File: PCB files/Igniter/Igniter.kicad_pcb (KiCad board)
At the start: 2 copper layers, 124.9 x 69.6 mm, 56 parts, among them IC1 74HC4050, J1 PT, J10 SL3, J11 SL4, J12 SL5, J13 Micro_SD_Card, J2 PT, J3 PT, J4 PT, J5 Battery, J6 Ignition Coil +, J7 Ignition coil -, J8 SL1, J9 SL2, Q1 N MOSFET, Q2 N MOSFET, Q3 N MOSFET, Q4 N MOSFET, Q5 N MOSFET, Q6 N MOSFET, SW1 ARM, U2 FDS8984, U3 FDS8984, U4 FDS8984

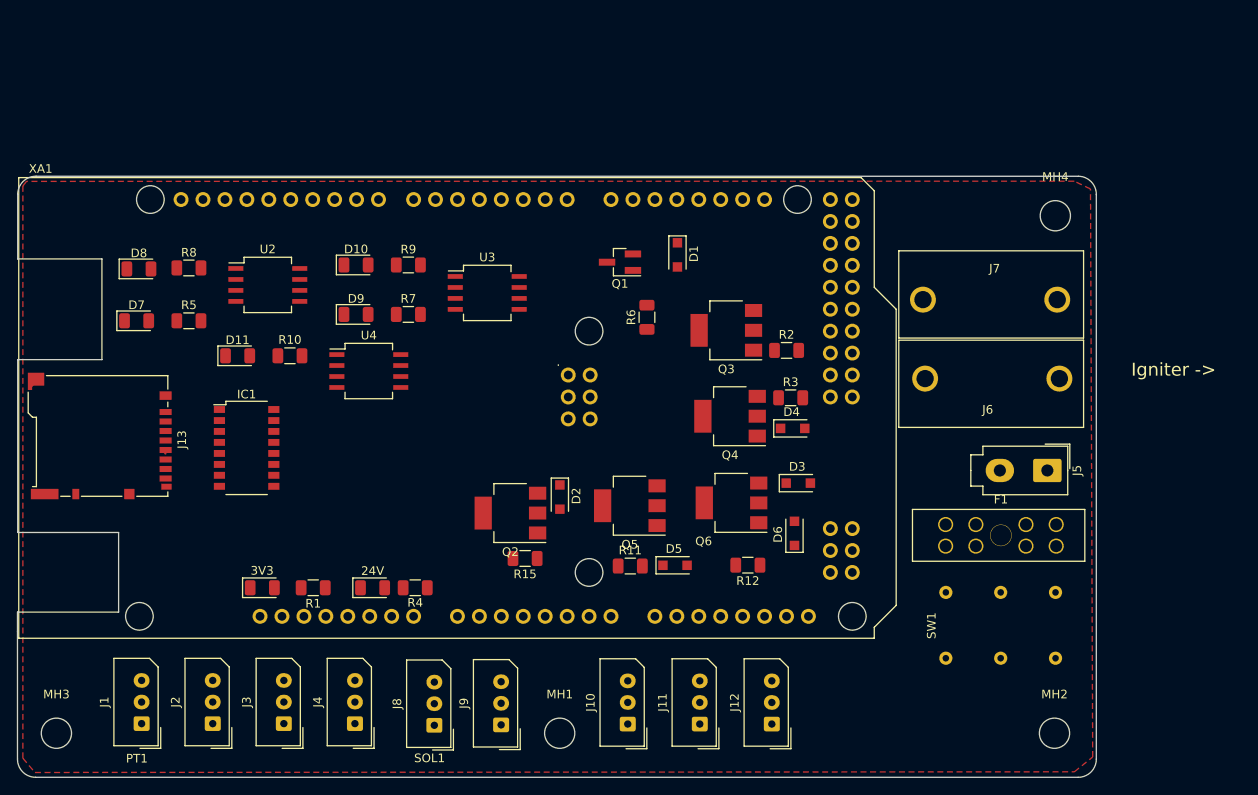
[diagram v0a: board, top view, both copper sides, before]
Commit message: 1/9/2019
-Set design rules to match with jlcpcb
-Began laying out power and some signal traces
-Changed FET symbol to 4pin to match sot223 footprint
Removed unused Arduino pins: (5V3,5V4,D22-D39)
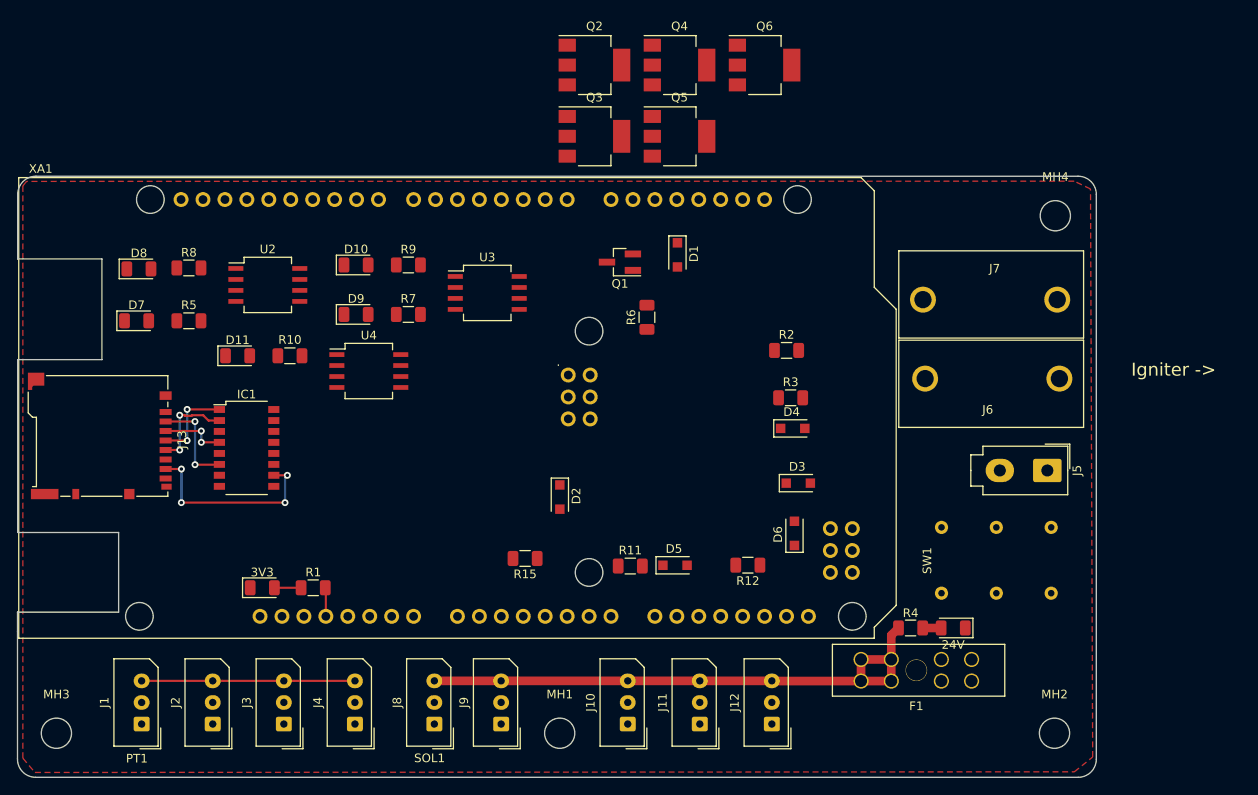
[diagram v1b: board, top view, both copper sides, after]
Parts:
- Q2, Q3, Q4, Q5, Q6: value N MOSFET -> Q_NMOS_GDSD
- moved D13 67.4 mm to (193.4, 138.4), turned to 180 degrees
- moved R4 57.6 mm to (188.5, 138.4), turned to 180 degrees
- moved Q2 52.8 mm to (151.9, 73.3), turned to 0 degrees
- moved Q6 50.8 mm to (171.6, 73.3), turned to 0 degrees
- moved Q5 43.2 mm to (161.7, 81.5), turned to 0 degrees
- moved Q4 41.1 mm to (161.7, 73.3), turned to 0 degrees
- moved Q3 27.2 mm to (151.9, 81.5), turned to 0 degrees
- moved F1 18.4 mm to (189.2, 143.3), turned to 0 degrees
- moved SW1 7.55 mm to (198.4, 130.6)
- moved J8 0.14 mm to (133.4, 149.6)
- moved J9 0.10 mm to (141.1, 149.6)
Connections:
- Q2 pad 4: (no net) -> Net-(D2-Pad2)
- Q3 pad 4: (no net) -> Net-(D3-Pad2)
- Q4 pad 4: (no net) -> Net-(D4-Pad2)
- Q5 pad 4: (no net) -> Net-(D5-Pad2)
- Q6 pad 4: (no net) -> Net-(D6-Pad2)
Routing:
- net +24V: track 0.00 -> 90.1 mm
- net Net-(IC1-Pad10): track 0.00 -> 22.6 mm, vias 0 -> 4
- net +3V3: track 0.11 -> 13.2 mm, vias 0 -> 2
- net Net-(IC1-Pad6): track 0.00 -> 11.2 mm, vias 0 -> 2
- net Net-(IC1-Pad2): track 0.00 -> 10.6 mm, vias 0 -> 2
- net Net-(IC1-Pad4): track 0.00 -> 7.54 mm, vias 0 -> 2
- net Net-(D12-Pad2): track 0.00 -> 3.09 mm
- net Net-(D13-Pad2): track 0.00 -> 2.14 mm
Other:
- board text added: "Trace direction: FRONT = Horizontal BACK = Vertical"
- board text removed: "Trace direction: FRONT = Vertical BACK = Horizontal"

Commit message: 1/14/2020
-Continued work on board routing
-Changed igniter connector footprint to have two pins to match banana jack connector
-Created GND plane on bottom layer
-Created footprint for rocker switch
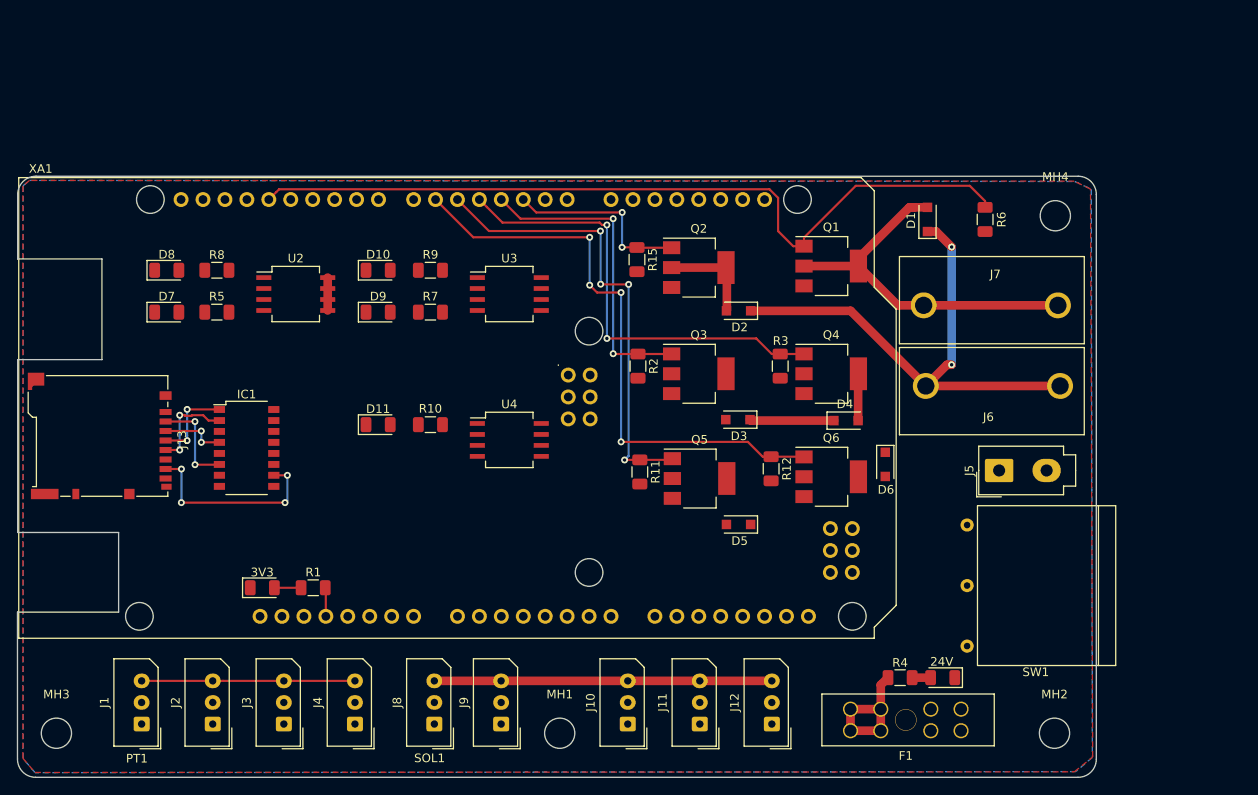
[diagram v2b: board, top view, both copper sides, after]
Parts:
- J6: value Ignition Coil + -> COIL
- J7: value Ignition coil - -> COIL
- Q1: value N MOSFET -> IGN; footprint Package_TO_SOT_SMD:SOT-23_Handsoldering -> Package_TO_SOT_SMD:SOT-223
- SW1: footprint IgniterFootprints:C&K_S101031MS02Q -> IgniterCustom:R1966ABLKBLKFR-SPST
- moved Q6 48.3 mm to (179.3, 120.9)
- moved R6 40.8 mm to (197.1, 91.1)
- moved Q4 39.8 mm to (179.3, 109.0)
- moved Q5 39.7 mm to (164.1, 121.1)
- moved R15 37.0 mm to (156.8, 95.8), turned to 270 degrees
- moved Q3 30.0 mm to (164.0, 109.0)
- moved D2 29.9 mm to (168.6, 101.7), turned to 180 degrees
- moved D1 29.2 mm to (190.5, 91.1), turned to 90 degrees
- moved Q2 26.4 mm to (164.0, 96.7)
- moved Q1 24.5 mm to (179.3, 96.5), turned to 0 degrees
- moved R10 18.1 mm to (132.9, 114.9)
- moved D11 18.1 mm to (126.8, 114.9)
- moved U4 18.1 mm to (142.0, 116.7)
- moved R2 17.3 mm to (156.9, 108.1), turned to 270 degrees
- moved D6 13.2 mm to (185.6, 119.5), turned to 270 degrees
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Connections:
- IC1 pad 12: Net-(IC1-Pad12) -> (no net)
- IC1 pad 13: Net-(IC1-Pad13) -> (no net)
- IC1 pad 15: Net-(IC1-Pad15) -> (no net)
- IC1 pad 16: Net-(IC1-Pad16) -> (no net)
- J13 pad 1: Net-(J13-Pad1) -> (no net)
- J13 pad 8: Net-(J13-Pad8) -> (no net)
- J13 pad 9: Net-(J13-Pad9) -> (no net)
- J6 pad 2: (no net) -> +24V
- J7 pad 2: (no net) -> Net-(D1-Pad2)
- U4 pad 3: Net-(U4-Pad3) -> (no net)
- U4 pad 4: Net-(U4-Pad4) -> (no net)
- U4 pad 5: Net-(U4-Pad5) -> (no net)
- U4 pad 6: Net-(U4-Pad6) -> (no net)
- XA1 pad 5V1: Net-(XA1-Pad5V1) -> (no net)
- XA1 pad 5V2: Net-(XA1-Pad5V2) -> (no net)
- XA1 pad A10: Net-(XA1-PadA10) -> (no net)
- XA1 pad A11: Net-(XA1-PadA11) -> (no net)
- XA1 pad A12: Net-(XA1-PadA12) -> (no net)
- XA1 pad A13: Net-(XA1-PadA13) -> (no net)
- XA1 pad A14: Net-(XA1-PadA14) -> (no net)
- XA1 pad A15: Net-(XA1-PadA15) -> (no net)
- XA1 pad A4: Net-(XA1-PadA4) -> (no net)
- XA1 pad A5: Net-(XA1-PadA5) -> (no net)
- XA1 pad A6: Net-(XA1-PadA6) -> (no net)
- XA1 pad A7: Net-(XA1-PadA7) -> (no net)
- XA1 pad A8: Net-(XA1-PadA8) -> (no net)
- XA1 pad A9: Net-(XA1-PadA9) -> (no net)
- XA1 pad AREF: Net-(XA1-PadAREF) -> (no net)
- XA1 pad D0: Net-(XA1-PadD0) -> (no net)
- XA1 pad D1: Net-(XA1-PadD1) -> (no net)
- XA1 pad D10: Net-(XA1-PadD10) -> (no net)
- XA1 pad D11: Net-(XA1-PadD11) -> (no net)
- XA1 pad D12: Net-(XA1-PadD12) -> (no net)
- XA1 pad D14: Net-(XA1-PadD14) -> (no net)
- XA1 pad D15: Net-(XA1-PadD15) -> (no net)
- XA1 pad D16: Net-(XA1-PadD16) -> (no net)
- XA1 pad D17: Net-(XA1-PadD17) -> (no net)
- XA1 pad D18: Net-(XA1-PadD18) -> (no net)
- XA1 pad D19: Net-(XA1-PadD19) -> (no net)
- XA1 pad D20: Net-(XA1-PadD20) -> (no net)
- XA1 pad D21: Net-(XA1-PadD21) -> (no net)
- XA1 pad D50: Net-(XA1-PadD50) -> (no net)
- XA1 pad D51: Net-(XA1-PadD51) -> (no net)
- XA1 pad D52: Net-(XA1-PadD52) -> (no net)
- XA1 pad D7: Net-(XA1-PadD7) -> (no net)
- XA1 pad D8: Net-(XA1-PadD8) -> (no net)
- XA1 pad D9: Net-(XA1-PadD9) -> (no net)
- XA1 pad IORF: Net-(XA1-PadIORF) -> (no net)
- XA1 pad RST1: Net-(XA1-PadRST1) -> (no net)
- XA1 pad RST2: Net-(XA1-PadRST2) -> (no net)
- XA1 pad SCL: Net-(XA1-PadSCL) -> (no net)
- XA1 pad SDA: Net-(XA1-PadSDA) -> (no net)
- XA1 pad VIN: Net-(XA1-PadVIN) -> (no net)
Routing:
- net Net-(Q1-Pad1): track 0.04 -> 93.4 mm
- net SOL5: track 0.00 -> 68.4 mm, vias 0 -> 4
- net +24V: track 90.1 -> 154.0 mm, vias 0 -> 2
- net SOL4: track 0.00 -> 53.6 mm, vias 0 -> 4
- net SOL3: track 0.00 -> 52.8 mm, vias 0 -> 2
- net Net-(D1-Pad2): track 0.00 -> 42.6 mm
- net SOL2: track 0.00 -> 36.3 mm, vias 0 -> 2
- net SOL1: track 0.00 -> 21.9 mm, vias 0 -> 2
- net Net-(D2-Pad2): track 0.00 -> 11.3 mm
- net Net-(D4-Pad2): track 0.00 -> 5.44 mm
- added copper zone on B.Cu, net GNDREF
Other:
- board text removed: "Igniter ->"

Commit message: 1/15/2020
Continued board routing work
-Swapped rocker switch terminals
-Grouped all board LEDs
-Changed PCB grid size to 10 mil
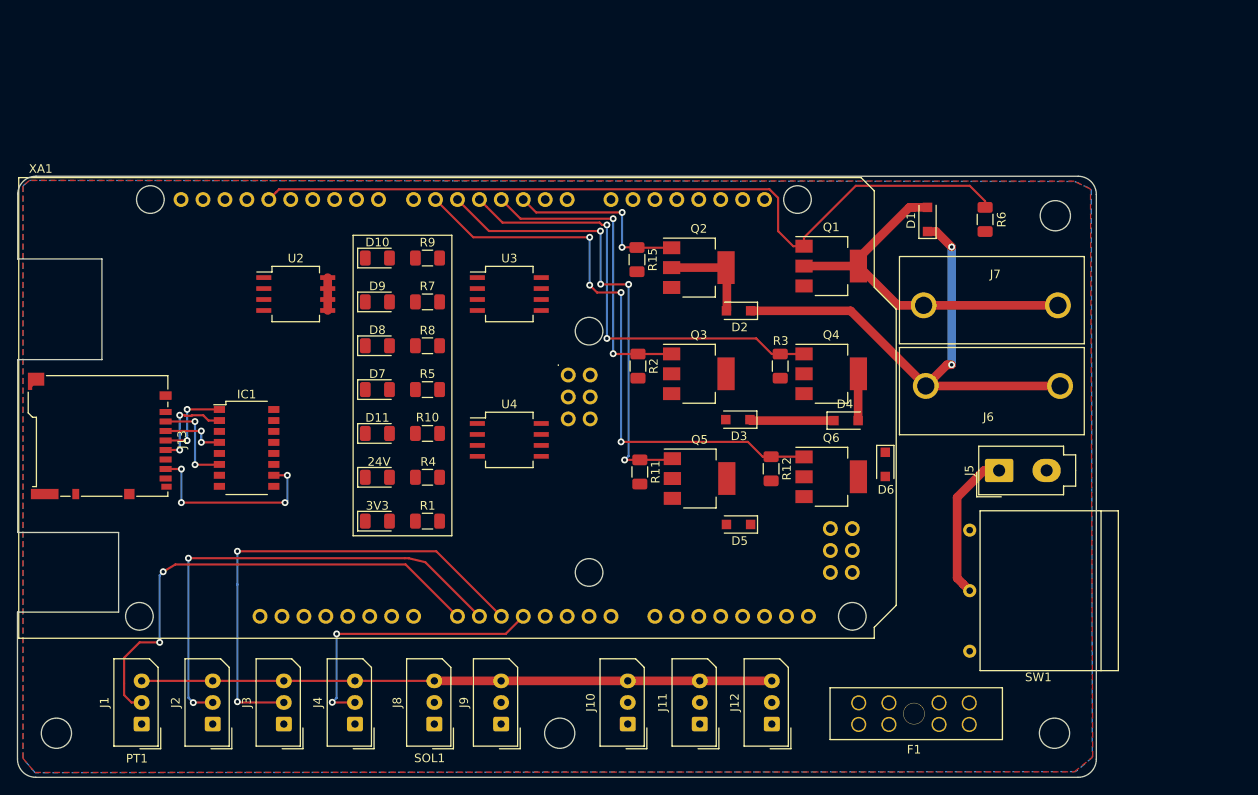
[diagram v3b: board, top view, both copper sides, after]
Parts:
- moved D13 69.4 mm to (126.8, 121.0), turned to 0 degrees
- moved R4 59.4 mm to (132.6, 121.0), turned to 0 degrees
- moved R5 26.0 mm to (132.6, 110.8)
- moved D7 26.0 mm to (126.8, 110.8)
- moved R8 25.9 mm to (132.6, 105.8)
- moved D8 25.9 mm to (126.8, 105.8)
- moved D12 15.4 mm to (126.8, 126.1)
- moved R1 15.3 mm to (132.6, 126.1)
- moved R9 1.45 mm to (132.6, 95.6)
- moved D10 1.41 mm to (126.8, 95.6)
- moved R7 1.23 mm to (132.6, 100.7)
- moved F1 1.19 mm to (188.9, 148.4)
- moved D9 1.19 mm to (126.8, 100.7)
- moved R10 1.07 mm to (132.6, 115.9)
- moved D11 1.02 mm to (126.8, 115.9)
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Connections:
- IC1 pad 12: (no net) -> Net-(IC1-Pad12)
- IC1 pad 13: (no net) -> Net-(IC1-Pad13)
- IC1 pad 15: (no net) -> Net-(IC1-Pad15)
- IC1 pad 16: (no net) -> Net-(IC1-Pad16)
- J13 pad 1: (no net) -> Net-(J13-Pad1)
- J13 pad 8: (no net) -> Net-(J13-Pad8)
- J13 pad 9: (no net) -> Net-(J13-Pad9)
- SW1 pad 1: Net-(J5-Pad1) -> Net-(F1-Pad5)
- SW1 pad 2: Net-(F1-Pad5) -> Net-(J5-Pad1)
- U4 pad 3: (no net) -> Net-(U4-Pad3)
- U4 pad 4: (no net) -> Net-(U4-Pad4)
- U4 pad 5: (no net) -> Net-(U4-Pad5)
- U4 pad 6: (no net) -> Net-(U4-Pad6)
- XA1 pad 5V1: (no net) -> Net-(XA1-Pad5V1)
- XA1 pad 5V2: (no net) -> Net-(XA1-Pad5V2)
- XA1 pad A10: (no net) -> Net-(XA1-PadA10)
- XA1 pad A11: (no net) -> Net-(XA1-PadA11)
- XA1 pad A12: (no net) -> Net-(XA1-PadA12)
- XA1 pad A13: (no net) -> Net-(XA1-PadA13)
- XA1 pad A14: (no net) -> Net-(XA1-PadA14)
- XA1 pad A15: (no net) -> Net-(XA1-PadA15)
- XA1 pad A4: (no net) -> Net-(XA1-PadA4)
- XA1 pad A5: (no net) -> Net-(XA1-PadA5)
- XA1 pad A6: (no net) -> Net-(XA1-PadA6)
- XA1 pad A7: (no net) -> Net-(XA1-PadA7)
- XA1 pad A8: (no net) -> Net-(XA1-PadA8)
- XA1 pad A9: (no net) -> Net-(XA1-PadA9)
- XA1 pad AREF: (no net) -> Net-(XA1-PadAREF)
- XA1 pad D0: (no net) -> Net-(XA1-PadD0)
- XA1 pad D1: (no net) -> Net-(XA1-PadD1)
- XA1 pad D10: (no net) -> Net-(XA1-PadD10)
- XA1 pad D11: (no net) -> Net-(XA1-PadD11)
- XA1 pad D12: (no net) -> Net-(XA1-PadD12)
- XA1 pad D14: (no net) -> Net-(XA1-PadD14)
- XA1 pad D15: (no net) -> Net-(XA1-PadD15)
- XA1 pad D16: (no net) -> Net-(XA1-PadD16)
- XA1 pad D17: (no net) -> Net-(XA1-PadD17)
- XA1 pad D18: (no net) -> Net-(XA1-PadD18)
- XA1 pad D19: (no net) -> Net-(XA1-PadD19)
- XA1 pad D20: (no net) -> Net-(XA1-PadD20)
- XA1 pad D21: (no net) -> Net-(XA1-PadD21)
- XA1 pad D50: (no net) -> Net-(XA1-PadD50)
- XA1 pad D51: (no net) -> Net-(XA1-PadD51)
- XA1 pad D52: (no net) -> Net-(XA1-PadD52)
- XA1 pad D7: (no net) -> Net-(XA1-PadD7)
- XA1 pad D8: (no net) -> Net-(XA1-PadD8)
- XA1 pad D9: (no net) -> Net-(XA1-PadD9)
- XA1 pad IORF: (no net) -> Net-(XA1-PadIORF)
- XA1 pad RST1: (no net) -> Net-(XA1-PadRST1)
- XA1 pad RST2: (no net) -> Net-(XA1-PadRST2)
- XA1 pad SCL: (no net) -> Net-(XA1-PadSCL)
- XA1 pad SDA: (no net) -> Net-(XA1-PadSDA)
- XA1 pad VIN: (no net) -> Net-(XA1-PadVIN)
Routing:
- net /PT0: track 0.00 -> 56.7 mm, vias 0 -> 2
- net /PT2: track 0.00 -> 56.5 mm, vias 0 -> 2
- net /PT1: track 0.00 -> 55.6 mm, vias 0 -> 2
- net /PT3: track 0.00 -> 33.2 mm, vias 0 -> 2
- net Net-(J5-Pad1): track 0.00 -> 17.6 mm
- net +24V: track 154.0 -> 147.2 mm
- net +3V3: track 13.2 -> 9.84 mm
- net Net-(D12-Pad2): track 3.09 -> 0.00 mm
- net Net-(D13-Pad2): track 2.14 -> 0.00 mm
